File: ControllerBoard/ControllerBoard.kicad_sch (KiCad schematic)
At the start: 0 parts

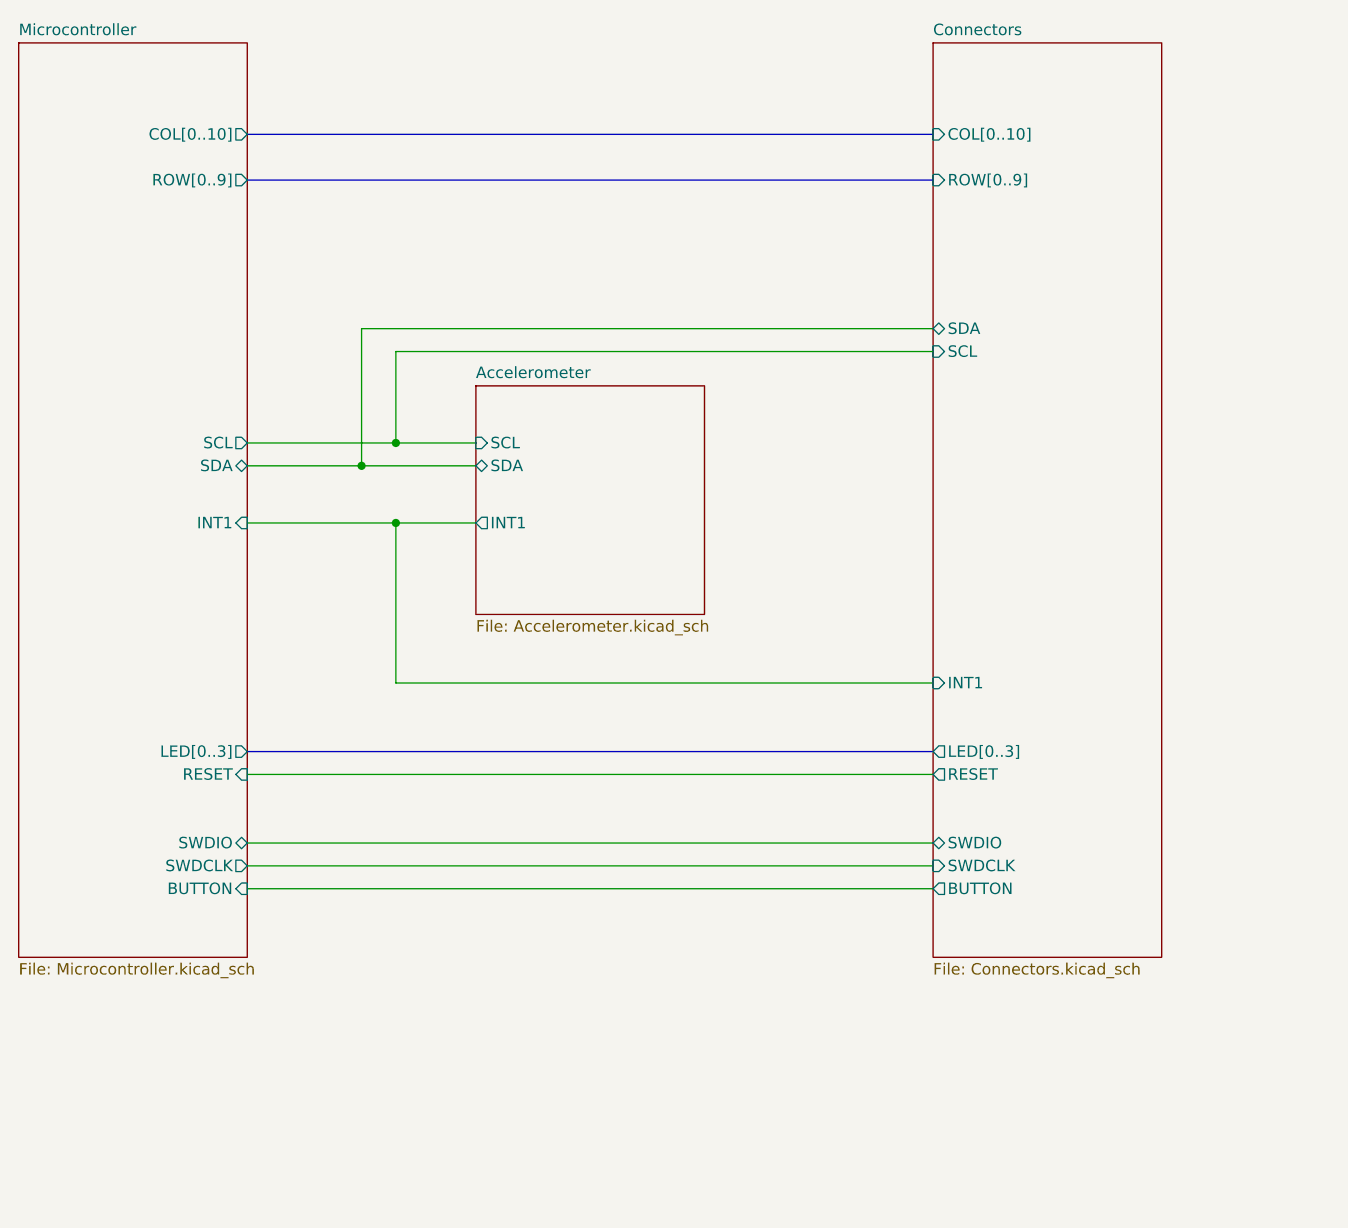
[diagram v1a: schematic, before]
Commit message: Change led matrix routing for sinking current through mcu, sourcing from battery
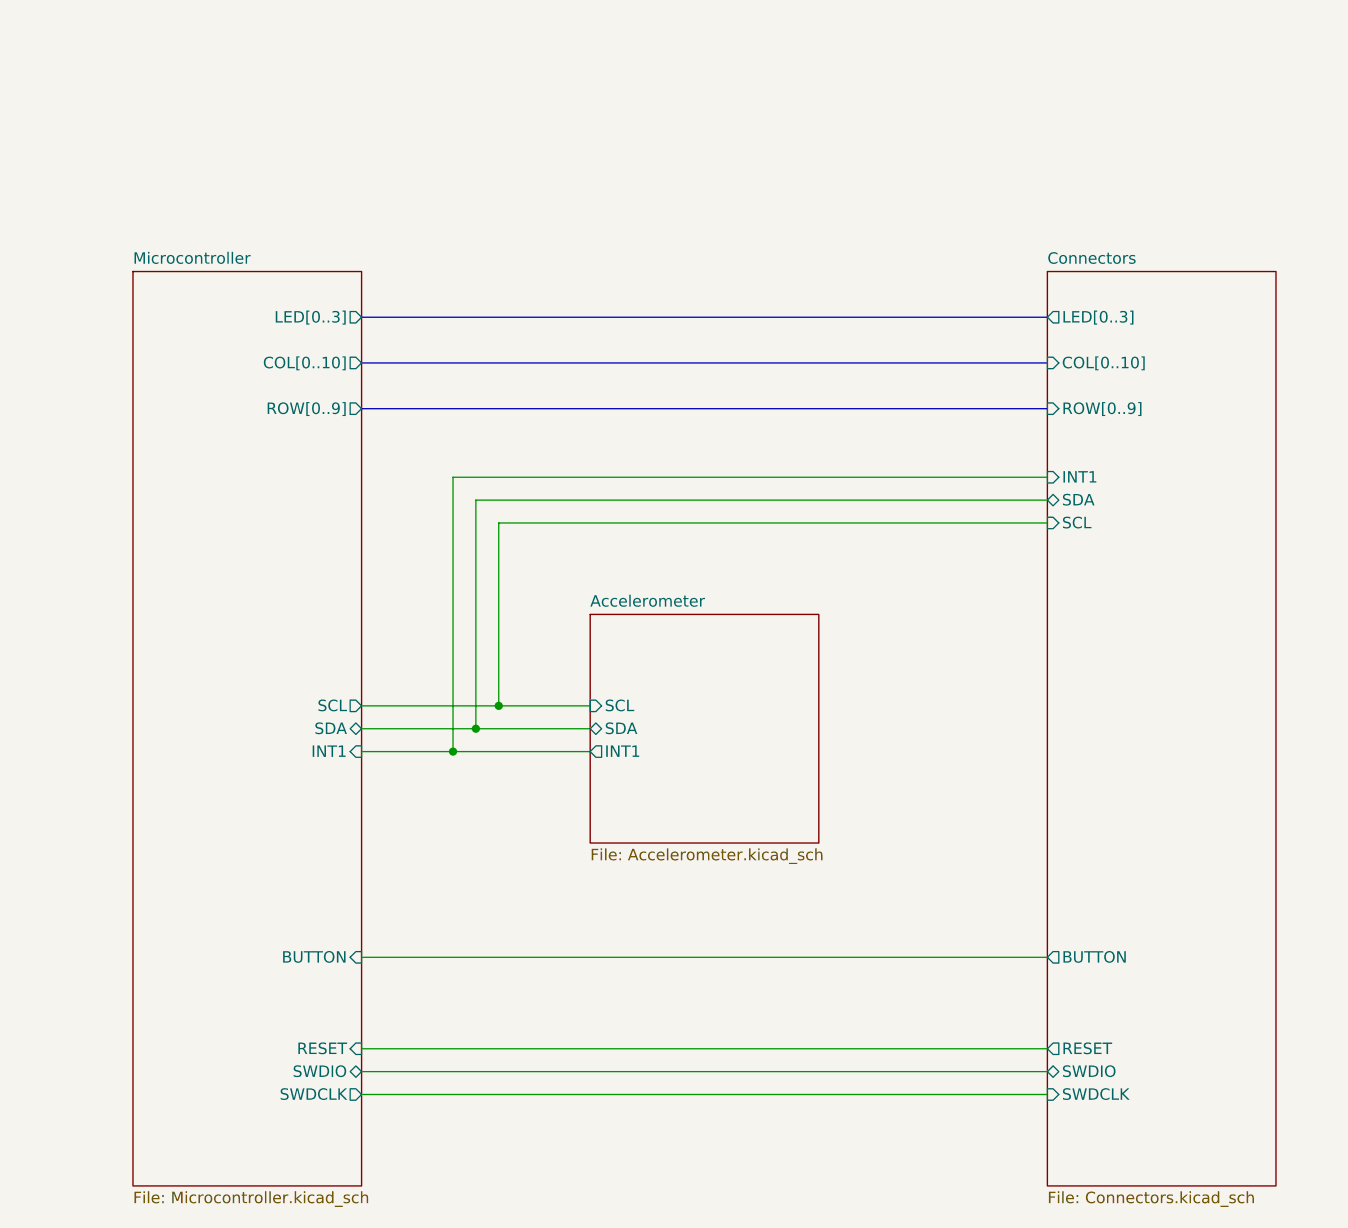
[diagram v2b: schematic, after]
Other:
- title: (none) -> WordWatch - Controller Board
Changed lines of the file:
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@@
 (kicad_sch (version 20230121) (generator eeschema)
   (paper "A4")
-  (junction (at 67.31 69.85) (diameter 0) (color 0 0 0 0)
+  (title_block
+    (title "WordWatch - Controller Board")
+    (date "2023-11-11")
+    (rev "1.0")
   )
-  (junction (at 63.5 72.39) (diameter 0) (color 0 0 0 0)
+  (junction (at 73.66 104.14) (diameter 0) (color 0 0 0 0)
   )
-  (junction (at 67.31 78.74) (diameter 0) (color 0 0 0 0)
+  (junction (at 78.74 99.06) (diameter 0) (color 0 0 0 0)
   )
-  (wire (pts (xy 50.8 78.74) (xy 67.31 78.74))
+  (junction (at 76.2 101.6) (diameter 0) (color 0 0 0 0)
+  )
+  (wire (pts (xy 63.5 104.14) (xy 73.66 104.14))
     (stroke (width 0) (type default))
   )
-  (bus (pts (xy 50.8 35.56) (xy 127 35.56))
+  (bus (pts (xy 63.5 60.96) (xy 139.7 60.96))
     (stroke (width 0) (type default))
   )
-  (wire (pts (xy 67.31 59.69) (xy 127 59.69))
+  (wire (pts (xy 78.74 78.74) (xy 139.7 78.74))
     (stroke (width 0) (type default))
   )
-  (wire (pts (xy 50.8 119.38) (xy 127 119.38))
+  (bus (pts (xy 63.5 55.88) (xy 139.7 55.88))
     (stroke (width 0) (type default))
   )
-  (wire (pts (xy 67.31 69.85) (xy 67.31 59.69))
+  (wire (pts (xy 76.2 76.2) (xy 76.2 101.6))
     (stroke (width 0) (type default))
   )
-  (wire (pts (xy 127 96.52) (xy 67.31 96.52))
+  (wire (pts (xy 63.5 127) (xy 139.7 127))
     (stroke (width 0) (type default))
   )
-  (wire (pts (xy 67.31 96.52) (xy 67.31 78.74))
+  (wire (pts (xy 78.74 78.74) (xy 78.74 99.06))
     (stroke (width 0) (type default))
   )
-  (bus (pts (xy 50.8 104.14) (xy 127 104.14))
+  (wire (pts (xy 139.7 73.66) (xy 73.66 73.66))
     (stroke (width 0) (type default))
   )
-  (wire (pts (xy 67.31 78.74) (xy 76.2 78.74))
+  (wire (pts (xy 73.66 73.66) (xy 73.66 104.14))
     (stroke (width 0) (type default))
   )
-  (wire (pts (xy 50.8 72.39) (xy 63.5 72.39))
+  (wire (pts (xy 73.66 104.14) (xy 88.9 104.14))
     (stroke (width 0) (type default))
   )
-  (bus (pts (xy 50.8 40.64) (xy 127 40.64))
+  (wire (pts (xy 63.5 101.6) (xy 76.2 101.6))
     (stroke (width 0) (type default))
   )
-  (wire (pts (xy 50.8 116.84) (xy 127 116.84))
+  (bus (pts (xy 63.5 66.04) (xy 139.7 66.04))
     (stroke (width 0) (type default))
   )
-  (wire (pts (xy 50.8 69.85) (xy 67.31 69.85))
+  (wire (pts (xy 63.5 142.24) (xy 139.7 142.24))
     (stroke (width 0) (type default))
   )
-  (wire (pts (xy 50.8 106.68) (xy 127 106.68))
+  (wire (pts (xy 63.5 99.06) (xy 78.74 99.06))
     (stroke (width 0) (type default))
   )
-  (wire (pts (xy 76.2 69.85) (xy 67.31 69.85))
+  (wire (pts (xy 63.5 137.16) (xy 139.7 137.16))
     (stroke (width 0) (type default))
   )
-  (wire (pts (xy 63.5 57.15) (xy 127 57.15))
+  (wire (pts (xy 78.74 99.06) (xy 88.9 99.06))
     (stroke (width 0) (type default))
   )
-  (wire (pts (xy 50.8 114.3) (xy 127 114.3))
+  (wire (pts (xy 76.2 76.2) (xy 139.7 76.2))
     (stroke (width 0) (type default))
   )
-  (wire (pts (xy 63.5 72.39) (xy 63.5 57.15))
+  (wire (pts (xy 63.5 139.7) (xy 139.7 139.7))
     (stroke (width 0) (type default))
   )
-  (wire (pts (xy 76.2 72.39) (xy 63.5 72.39))
+  (wire (pts (xy 88.9 101.6) (xy 76.2 101.6))
     (stroke (width 0) (type default))
   )
-  (sheet (at 127 25.4) (size 25.4 101.6) (fields_autoplaced)
+  (sheet (at 139.7 50.8) (size 25.4 101.6) (fields_autoplaced)
     (stroke (width 0.1524) (type solid))
     (fill (color 0 0 0 0.0000))
-    (property "Sheetname" "Connectors" (at 127 24.6884 0)
+    (property "Sheetname" "Connectors" (at 139.7 50.0884 0)
       (effects (font (size 1.27 1.27)) (justify left bottom))
     )
-    (property "Sheetfile" "Connectors.kicad_sch" (at 127 127.5846 0)
+    (property "Sheetfile" "Connectors.kicad_sch" (at 139.7 152.9846 0)
       (effects (font (size 1.27 1.27)) (justify left top))
     )
-    (pin "ROW[0..9]" input (at 127 40.64 180)
+    (pin "ROW[0..9]" input (at 139.7 66.04 180)
       (effects (font (size 1.27 1.27)) (justify left))
     )
-    (pin "COL[0..10]" input (at 127 35.56 180)
+    (pin "COL[0..10]" input (at 139.7 60.96 180)
       (effects (font (size 1.27 1.27)) (justify left))
     )
-    (pin "SWDCLK" input (at 127 116.84 180)
+    (pin "SWDCLK" input (at 139.7 142.24 180)
       (effects (font (size 1.27 1.27)) (justify left))
     )
-    (pin "SWDIO" bidirectional (at 127 114.3 180)
+    (pin "SWDIO" bidirectional (at 139.7 139.7 180)
       (effects (font (size 1.27 1.27)) (justify left))
     )
-    (pin "RESET" output (at 127 106.68 180)
+    (pin "RESET" output (at 139.7 137.16 180)
       (effects (font (size 1.27 1.27)) (justify left))
     )
-    (pin "SCL" input (at 127 59.69 180)
+    (pin "SCL" input (at 139.7 78.74 180)
       (effects (font (size 1.27 1.27)) (justify left))
     )
-    (pin "BUTTON" output (at 127 119.38 180)
+    (pin "BUTTON" output (at 139.7 127 180)
       (effects (font (size 1.27 1.27)) (justify left))
     )
-    (pin "SDA" bidirectional (at 127 57.15 180)
+    (pin "SDA" bidirectional (at 139.7 76.2 180)
       (effects (font (size 1.27 1.27)) (justify left))
     )
-    (pin "LED[0..3]" output (at 127 104.14 180)
+    (pin "LED[0..3]" output (at 139.7 55.88 180)
       (effects (font (size 1.27 1.27)) (justify left))
     )
-    (pin "INT1" input (at 127 96.52 180)
+    (pin "INT1" input (at 139.7 73.66 180)
       (effects (font (size 1.27 1.27)) (justify left))
     )
@@
     )
   )
-  (sheet (at 25.4 25.4) (size 25.4 101.6) (fields_autoplaced)
+  (sheet (at 38.1 50.8) (size 25.4 101.6) (fields_autoplaced)
     (stroke (width 0.1524) (type solid))
     (fill (color 0 0 0 0.0000))
-    (property "Sheetname" "Microcontroller" (at 25.4 24.6884 0)
+    (property "Sheetname" "Microcontroller" (at 38.1 50.0884 0)
       (effects (font (size 1.27 1.27)) (justify left bottom))
     )
-    (property "Sheetfile" "Microcontroller.kicad_sch" (at 25.4 127.5846 0)
+    (property "Sheetfile" "Microcontroller.kicad_sch" (at 38.1 152.9846 0)
       (effects (font (size 1.27 1.27)) (justify left top))
     )
-    (pin "SDA" bidirectional (at 50.8 72.39 0)
+    (pin "SDA" bidirectional (at 63.5 101.6 0)
       (effects (font (size 1.27 1.27)) (justify right))
     )
-    (pin "SCL" output (at 50.8 69.85 0)
+    (pin "SCL" output (at 63.5 99.06 0)
       (effects (font (size 1.27 1.27)) (justify right))
     )
-    (pin "LED[0..3]" output (at 50.8 104.14 0)
+    (pin "LED[0..3]" output (at 63.5 55.88 0)
       (effects (font (size 1.27 1.27)) (justify right))
     )
-    (pin "BUTTON" input (at 50.8 119.38 0)
+    (pin "BUTTON" input (at 63.5 127 0)
       (effects (font (size 1.27 1.27)) (justify right))
     )
-    (pin "INT1" input (at 50.8 78.74 0)
+    (pin "INT1" input (at 63.5 104.14 0)
       (effects (font (size 1.27 1.27)) (justify right))
     )
-    (pin "SWDCLK" output (at 50.8 116.84 0)
+    (pin "SWDCLK" output (at 63.5 142.24 0)
       (effects (font (size 1.27 1.27)) (justify right))
     )
-    (pin "SWDIO" bidirectional (at 50.8 114.3 0)
+    (pin "SWDIO" bidirectional (at 63.5 139.7 0)
       (effects (font (size 1.27 1.27)) (justify right))
     )
-    (pin "RESET" input (at 50.8 106.68 0)
+    (pin "RESET" input (at 63.5 137.16 0)
       (effects (font (size 1.27 1.27)) (justify right))
     )
-    (pin "ROW[0..9]" output (at 50.8 40.64 0)
+    (pin "ROW[0..9]" output (at 63.5 66.04 0)
       (effects (font (size 1.27 1.27)) (justify right))
     )
-    (pin "COL[0..10]" output (at 50.8 35.56 0)
+    (pin "COL[0..10]" output (at 63.5 60.96 0)
       (effects (font (size 1.27 1.27)) (justify right))
     )
@@
     )
   )
-  (sheet (at 76.2 63.5) (size 25.4 25.4) (fields_autoplaced)
+  (sheet (at 88.9 88.9) (size 25.4 25.4) (fields_autoplaced)
     (stroke (width 0.1524) (type solid))
     (fill (color 0 0 0 0.0000))
-    (property "Sheetname" "Accelerometer" (at 76.2 62.7884 0)
+    (property "Sheetname" "Accelerometer" (at 88.9 88.1884 0)
       (effects (font (size 1.27 1.27)) (justify left bottom))
     )
-    (property "Sheetfile" "Accelerometer.kicad_sch" (at 76.2 89.4846 0)
+    (property "Sheetfile" "Accelerometer.kicad_sch" (at 88.9 114.8846 0)
       (effects (font (size 1.27 1.27)) (justify left top))
     )
-    (pin "INT1" output (at 76.2 78.74 180)
+    (pin "INT1" output (at 88.9 104.14 180)
       (effects (font (size 1.27 1.27)) (justify left))
     )
-    (pin "SDA" bidirectional (at 76.2 72.39 180)
+    (pin "SDA" bidirectional (at 88.9 101.6 180)
       (effects (font (size 1.27 1.27)) (justify left))
     )
-    (pin "SCL" input (at 76.2 69.85 180)
+    (pin "SCL" input (at 88.9 99.06 180)
       (effects (font (size 1.27 1.27)) (justify left))
     )
